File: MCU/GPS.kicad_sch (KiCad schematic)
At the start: 12 parts, among them J801 Conn_Coaxial, U801 NEO-M9N

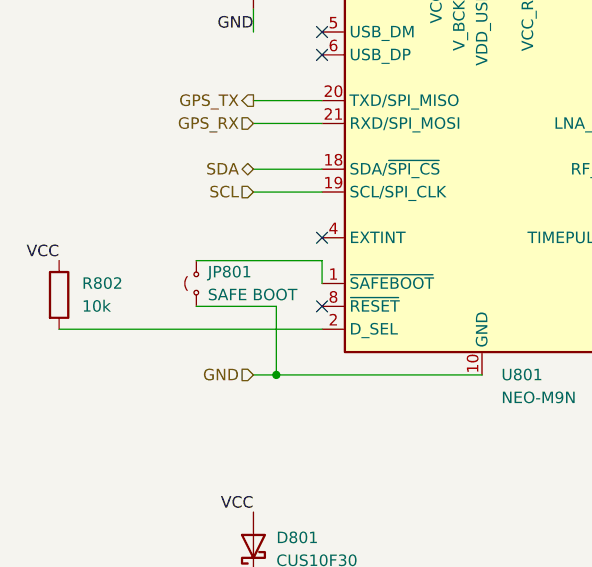
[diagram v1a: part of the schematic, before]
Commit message: Update: コネクタをだいぶ消した
手配線になるね
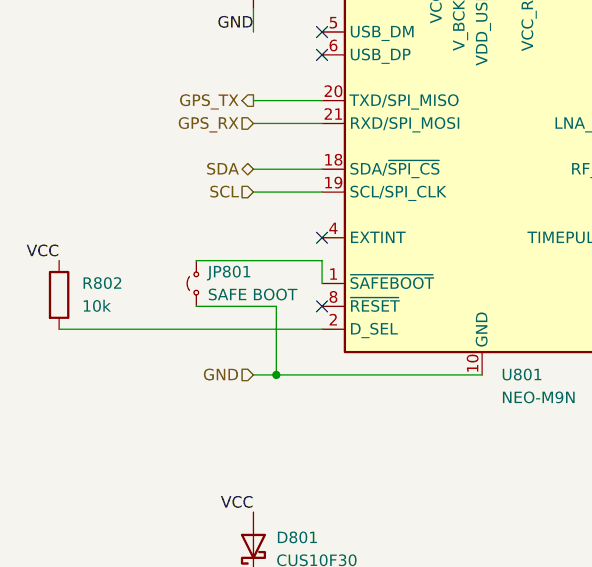
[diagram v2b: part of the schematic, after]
